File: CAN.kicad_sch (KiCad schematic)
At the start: 18 parts, among them J10 Conn_01x02, J8 CAN_IN, J9 CAN_OUT, U6 ADM3055E, U7 CDSOT23-T24CAN

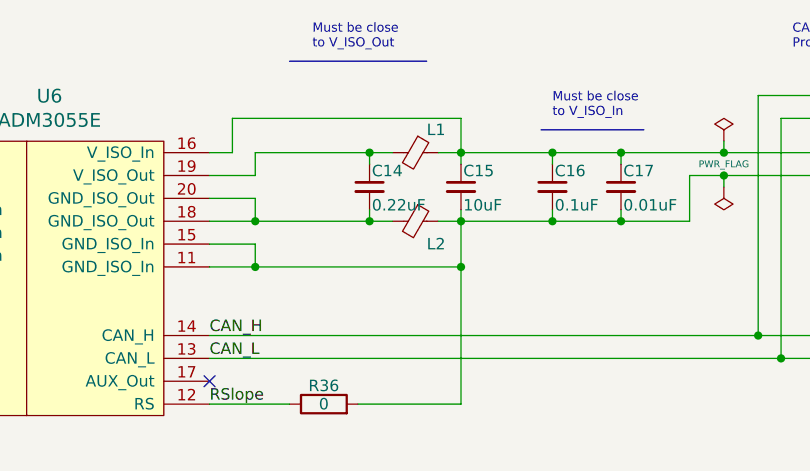
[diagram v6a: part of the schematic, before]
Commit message: changed more resistor values on SCH
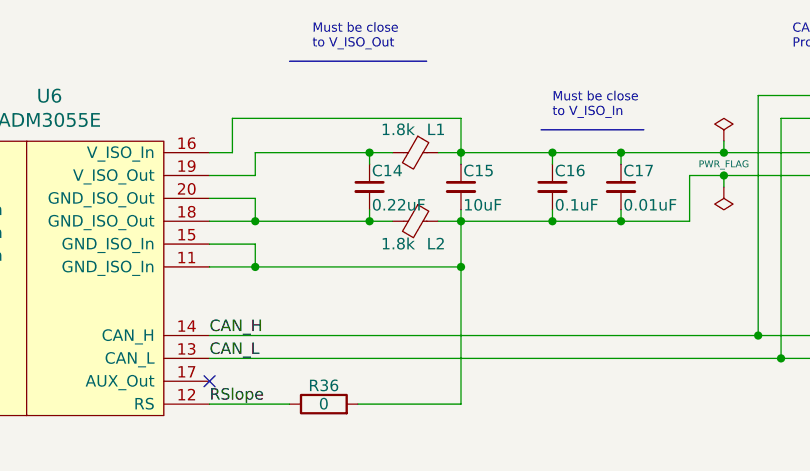
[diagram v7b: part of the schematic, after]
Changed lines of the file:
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@@
 				)
 				(justify left)
-				(hide yes)
 			)
 		)
@@
 				)
 				(justify left)
-				(hide yes)
-			)
-		)
+			)
+		)

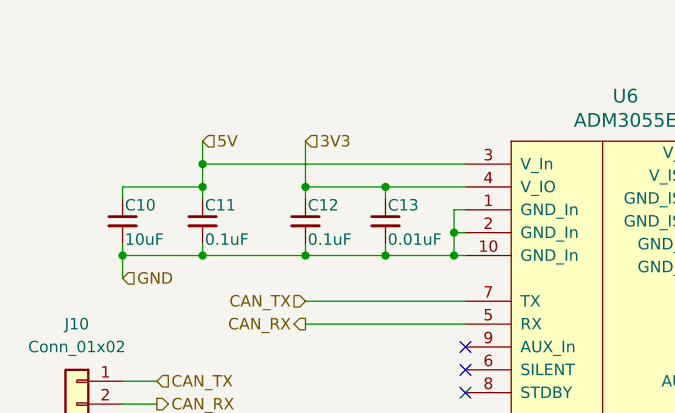
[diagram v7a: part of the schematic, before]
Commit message: emergency m_enable fix
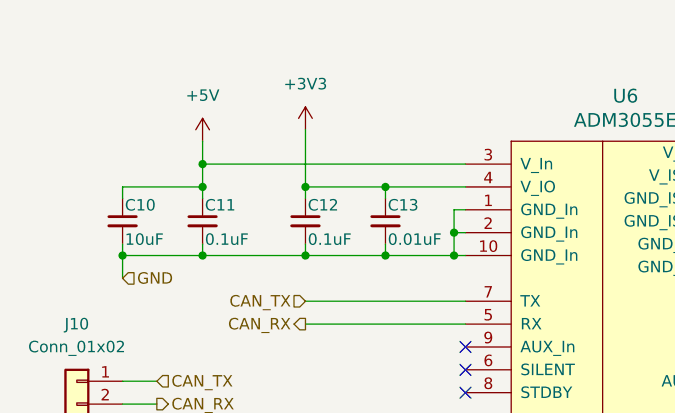
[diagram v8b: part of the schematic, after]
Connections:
- net 3V3 renamed +3V3
- net 5V renamed +5V
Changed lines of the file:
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@@
+	(wire
+		(pts
+			(xy 63.5 72.39) (xy 63.5 78.74)
+		)
+		(stroke
+			(width 0)
+			(type default)
+		)
+	)
 	(wire
 		(pts
@@
 		(pts
 			(xy 170.18 77.47) (xy 173.99 77.47)
-		)
-		(stroke
-			(width 0)
-			(type default)
-		)
-	)
-	(wire
-		(pts
-			(xy 63.5 73.66) (xy 63.5 78.74)
 		)
 		(stroke
@@
 			)
 			(justify left bottom)
-		)
-	)
-	(hierarchical_label "5V"
-		(shape input)
-		(at 52.07 73.66 0)
-		(fields_autoplaced yes)
-		(effects
-			(font
-				(size 1.27 1.27)
-			)
-			(justify left)
 		)
 	)
@@
 		)
 	)
-	(hierarchical_label "3V3"
-		(shape input)
-		(at 63.5 73.66 0)
-		(fields_autoplaced yes)
-		(effects
-			(font
-				(size 1.27 1.27)
-			)
-			(justify left)
-		)
-	)
 	(hierarchical_label "GND"
 		(shape input)
@@
 			)
 			(justify right)
+		)
+	)
+	(symbol
+		(lib_id "power:+5V")
+		(at 52.07 73.66 0)
+		(unit 1)
+		(exclude_from_sim no)
+		(in_bom yes)
+		(on_board yes)
+		(dnp no)
+		(fields_autoplaced yes)
+		(property "Reference" "#PWR021"
+			(at 52.07 77.47 0)
+			(effects
+				(font
+					(size 1.27 1.27)
+				)
+				(hide yes)
+			)
+		)
+		(property "Value" "+5V"
+			(at 52.07 68.58 0)
+			(effects
+				(font
+					(size 1.27 1.27)
+				)
+			)
+		)
+		(property "Footprint" ""
+			(at 52.07 73.66 0)
+			(effects
+				(font
+					(size 1.27 1.27)
+				)
+				(hide yes)
+			)
+		)
+		(property "Datasheet" ""
+			(at 52.07 73.66 0)
+			(effects
+				(font
+					(size 1.27 1.27)
+				)
+				(hide yes)
+			)
+		)
+		(property "Description" "Power symbol creates a global label with name \"+5V\""
+			(at 52.07 73.66 0)
+			(effects
+				(font
+					(size 1.27 1.27)
+				)
+				(hide yes)
+			)
+		)
+		(pin "1"
+		)
+		(instances
+			(project ""
+				(path "/b9847a31-2b3b-47ca-9561-fab506416f6d/a2982df7-4a65-4a2b-8298-6a7a639680dd"
+					(reference "#PWR021")
+					(unit 1)
+				)
+			)
 		)
 	)
@@
 					(unit 1)
 				)
+			)
+		)
+	)
+	(symbol
+		(lib_id "power:+3V3")
+		(at 63.5 72.39 0)
+		(unit 1)
+		(exclude_from_sim no)
+		(in_bom yes)
+		(on_board yes)
+		(dnp no)
+		(fields_autoplaced yes)
+		(property "Reference" "#PWR022"
+			(at 63.5 76.2 0)
+			(effects
+				(font
+					(size 1.27 1.27)
+				)
+				(hide yes)
+			)
+		)
+		(property "Value" "+3V3"
+			(at 63.5 67.31 0)
+			(effects
+				(font
+					(size 1.27 1.27)
+				)
+			)
+		)
+		(property "Footprint" ""
+			(at 63.5 72.39 0)
+			(effects
+				(font
+					(size 1.27 1.27)
+				)
+				(hide yes)
+			)
+		)
+		(property "Datasheet" ""
+			(at 63.5 72.39 0)
+			(effects
+				(font
+					(size 1.27 1.27)
+				)
+				(hide yes)
+			)
+		)
+		(property "Description" "Power symbol creates a global label with name \"+3V3\""
+			(at 63.5 72.39 0)
+			(effects
+				(font
+					(size 1.27 1.27)
+				)
+				(hide yes)
+			)
+		)
+		(pin "1"
+		)
+		(instances
+			(project ""
+				(path "/b9847a31-2b3b-47ca-9561-fab506416f6d/a2982df7-4a65-4a2b-8298-6a7a639680dd"
+					(reference "#PWR022")
+					(unit 1)
+				)
